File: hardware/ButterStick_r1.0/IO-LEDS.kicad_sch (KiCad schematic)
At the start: 20 parts, among them Q1 Q_NMOS_GSD, Q2 Q_NMOS_GSD, Q3 Q_NMOS_GSD

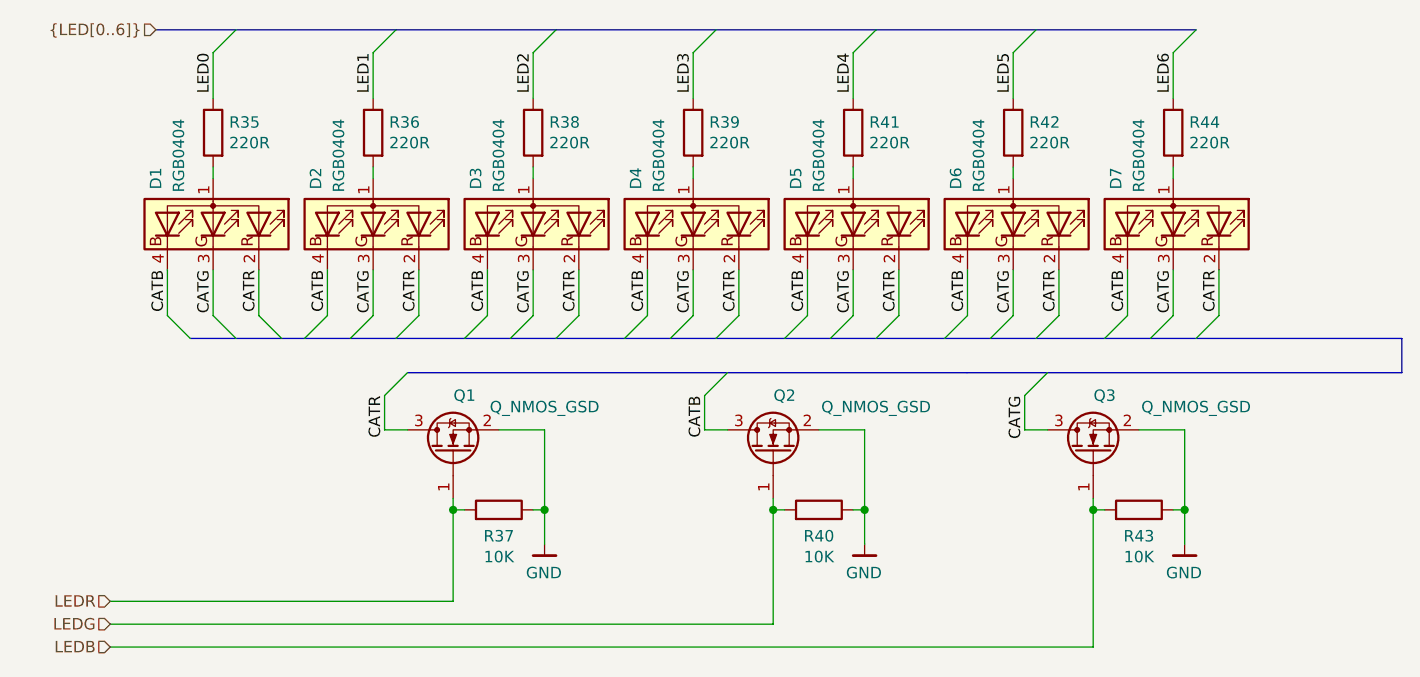
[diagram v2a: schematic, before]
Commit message: hw.r1d0: Fix RGMII straps
This commit correctly sets the stop resistos on the RGMII lines to 1K5
instead of DNP.
Also regenerate and add a schematic in PDF format.

Fixes #6
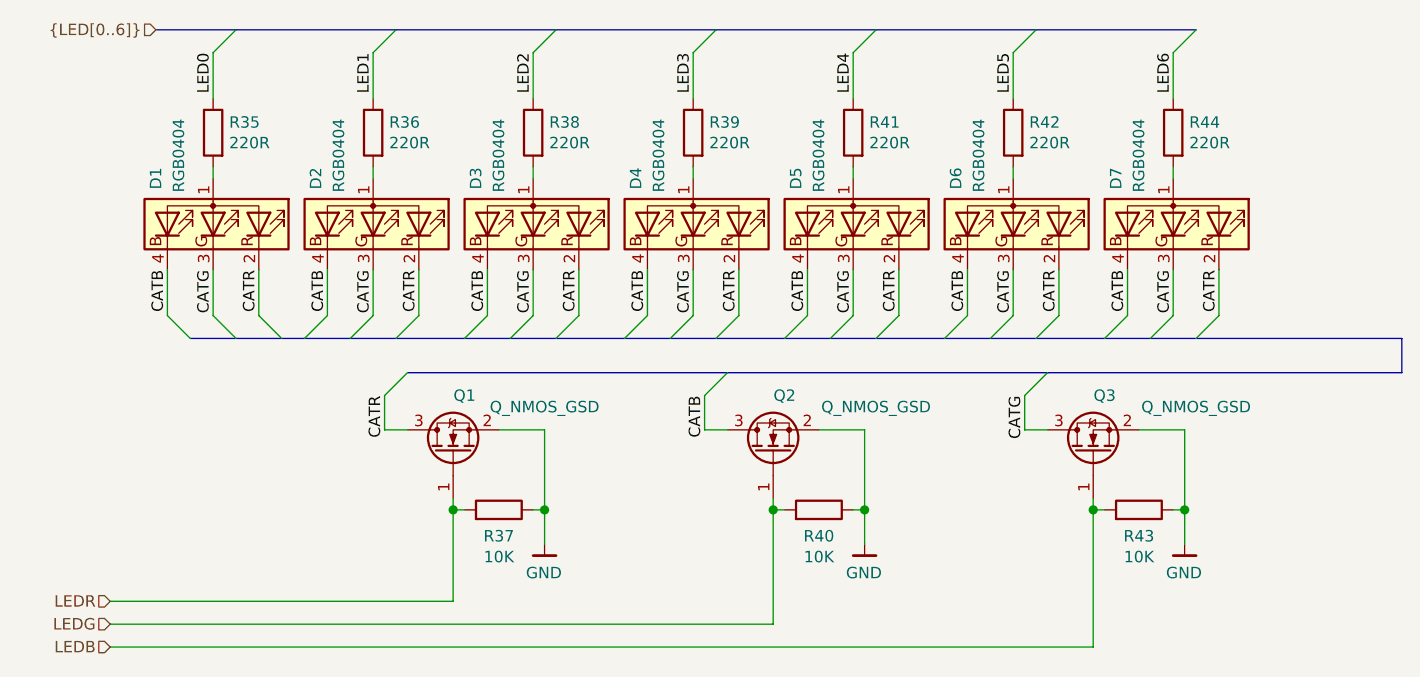
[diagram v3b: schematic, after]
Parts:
- D1, D2, D3, D4, D5, D6, D7: Mfg Foshan NationStar -> MEIHUA; PN FC-B1010RGBT-HG -> MHPA1010RGBDT
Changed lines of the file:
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@@
-(kicad_sch (version 20200618) (host eeschema "5.99.0-unknown-73168a9~101~ubuntu18.04.1")
+(kicad_sch (version 20201015) (generator eeschema)
   (page 1 18)
   (paper "A4")
   (title_block
     (title "ButterStick")
-    (date "2020-07-17")
+    (date "2020-11-01")
     (rev "r1.0")
     (company "GsD")
     (comment 1 "Functional prototyping board for the Lattice ECP5.")
-  )
-  (junction (at 116.84 125.73) (diameter 0) (color 0 0 0 0))
-  (junction (at 127 125.73) (diameter 0) (color 0 0 0 0))
-  (junction (at 152.4 125.73) (diameter 0) (color 0 0 0 0))
-  (junction (at 162.56 125.73) (diameter 0) (color 0 0 0 0))
-  (junction (at 187.96 125.73) (diameter 0) (color 0 0 0 0))
-  (junction (at 198.12 125.73) (diameter 0) (color 0 0 0 0))
+    (comment 2 "SYZYGY compatible")
+  )
+  (junction (at 116.84 125.73) (diameter 1.016) (color 0 0 0 0))
+  (junction (at 127 125.73) (diameter 1.016) (color 0 0 0 0))
+  (junction (at 152.4 125.73) (diameter 1.016) (color 0 0 0 0))
+  (junction (at 162.56 125.73) (diameter 1.016) (color 0 0 0 0))
+  (junction (at 187.96 125.73) (diameter 1.016) (color 0 0 0 0))
+  (junction (at 198.12 125.73) (diameter 1.016) (color 0 0 0 0))
   (bus_entry (at 85.09 104.14) (size 2.54 2.54)
     (stroke (width 0.1524) (type solid) (color 0 0 0 0))
@@
     (stroke (width 0) (type solid) (color 0 0 0 0))
   )
-  (bus (pts (xy 83.82 72.39) (xy 110.49 72.39))
-    (stroke (width 0) (type solid) (color 0 0 0 0))
-  )
-  (bus (pts (xy 87.63 106.68) (xy 97.79 106.68))
+  (bus (pts (xy 83.82 72.39) (xy 92.71 72.39))
+    (stroke (width 0) (type solid) (color 0 0 0 0))
+  )
+  (bus (pts (xy 87.63 106.68) (xy 92.71 106.68))
+    (stroke (width 0) (type solid) (color 0 0 0 0))
+  )
+  (bus (pts (xy 92.71 72.39) (xy 110.49 72.39))
+    (stroke (width 0) (type solid) (color 0 0 0 0))
+  )
+  (bus (pts (xy 92.71 106.68) (xy 97.79 106.68))
     (stroke (width 0) (type solid) (color 0 0 0 0))
   )
@@
     (stroke (width 0) (type solid) (color 0 0 0 0))
   )
-  (bus (pts (xy 100.33 106.68) (xy 110.49 106.68))
+  (bus (pts (xy 100.33 106.68) (xy 105.41 106.68))
+    (stroke (width 0) (type solid) (color 0 0 0 0))
+  )
+  (bus (pts (xy 105.41 106.68) (xy 110.49 106.68))
     (stroke (width 0) (type solid) (color 0 0 0 0))
   )
@@
     (stroke (width 0) (type solid) (color 0 0 0 0))
   )
-  (bus (pts (xy 111.76 110.49) (xy 173.99 110.49))
-    (stroke (width 0) (type solid) (color 0 0 0 0))
-  )
-  (bus (pts (xy 118.11 106.68) (xy 128.27 106.68))
-    (stroke (width 0) (type solid) (color 0 0 0 0))
-  )
-  (bus (pts (xy 128.27 72.39) (xy 163.83 72.39))
+  (bus (pts (xy 111.76 110.49) (xy 147.32 110.49))
+    (stroke (width 0) (type solid) (color 0 0 0 0))
+  )
+  (bus (pts (xy 118.11 106.68) (xy 123.19 106.68))
+    (stroke (width 0) (type solid) (color 0 0 0 0))
+  )
+  (bus (pts (xy 123.19 106.68) (xy 128.27 106.68))
+    (stroke (width 0) (type solid) (color 0 0 0 0))
+  )
+  (bus (pts (xy 128.27 72.39) (xy 146.05 72.39))
     (stroke (width 0) (type solid) (color 0 0 0 0))
   )
@@
     (stroke (width 0) (type solid) (color 0 0 0 0))
   )
-  (bus (pts (xy 135.89 106.68) (xy 146.05 106.68))
-    (stroke (width 0) (type solid) (color 0 0 0 0))
-  )
-  (bus (pts (xy 146.05 106.68) (xy 158.75 106.68))
-    (stroke (width 0) (type solid) (color 0 0 0 0))
-  )
-  (bus (pts (xy 158.75 106.68) (xy 171.45 106.68))
-    (stroke (width 0) (type solid) (color 0 0 0 0))
-  )
-  (bus (pts (xy 163.83 72.39) (xy 199.39 72.39))
-    (stroke (width 0) (type solid) (color 0 0 0 0))
-  )
-  (bus (pts (xy 171.45 106.68) (xy 181.61 106.68))
-    (stroke (width 0) (type solid) (color 0 0 0 0))
-  )
-  (bus (pts (xy 173.99 110.49) (xy 222.25 110.49))
-    (stroke (width 0) (type solid) (color 0 0 0 0))
-  )
-  (bus (pts (xy 181.61 106.68) (xy 194.31 106.68))
-    (stroke (width 0) (type solid) (color 0 0 0 0))
-  )
-  (bus (pts (xy 194.31 106.68) (xy 222.25 106.68))
+  (bus (pts (xy 135.89 106.68) (xy 140.97 106.68))
+    (stroke (width 0) (type solid) (color 0 0 0 0))
+  )
+  (bus (pts (xy 140.97 106.68) (xy 146.05 106.68))
+    (stroke (width 0) (type solid) (color 0 0 0 0))
+  )
+  (bus (pts (xy 146.05 72.39) (xy 163.83 72.39))
+    (stroke (width 0) (type solid) (color 0 0 0 0))
+  )
+  (bus (pts (xy 146.05 106.68) (xy 153.67 106.68))
+    (stroke (width 0) (type solid) (color 0 0 0 0))
+  )
+  (bus (pts (xy 147.32 110.49) (xy 182.88 110.49))
+    (stroke (width 0) (type solid) (color 0 0 0 0))
+  )
+  (bus (pts (xy 153.67 106.68) (xy 158.75 106.68))
+    (stroke (width 0) (type solid) (color 0 0 0 0))
+  )
+  (bus (pts (xy 158.75 106.68) (xy 163.83 106.68))
+    (stroke (width 0) (type solid) (color 0 0 0 0))
+  )
+  (bus (pts (xy 163.83 72.39) (xy 181.61 72.39))
+    (stroke (width 0) (type solid) (color 0 0 0 0))
+  )
+  (bus (pts (xy 163.83 106.68) (xy 171.45 106.68))
+    (stroke (width 0) (type solid) (color 0 0 0 0))
+  )
+  (bus (pts (xy 171.45 106.68) (xy 176.53 106.68))
+    (stroke (width 0) (type solid) (color 0 0 0 0))
+  )
+  (bus (pts (xy 176.53 106.68) (xy 181.61 106.68))
+    (stroke (width 0) (type solid) (color 0 0 0 0))
+  )
+  (bus (pts (xy 181.61 72.39) (xy 199.39 72.39))
+    (stroke (width 0) (type solid) (color 0 0 0 0))
+  )
+  (bus (pts (xy 181.61 106.68) (xy 189.23 106.68))
+    (stroke (width 0) (type solid) (color 0 0 0 0))
+  )
+  (bus (pts (xy 182.88 110.49) (xy 222.25 110.49))
+    (stroke (width 0) (type solid) (color 0 0 0 0))
+  )
+  (bus (pts (xy 189.23 106.68) (xy 194.31 106.68))
+    (stroke (width 0) (type solid) (color 0 0 0 0))
+  )
+  (bus (pts (xy 194.31 106.68) (xy 199.39 106.68))
+    (stroke (width 0) (type solid) (color 0 0 0 0))
+  )
+  (bus (pts (xy 199.39 106.68) (xy 222.25 106.68))
     (stroke (width 0) (type solid) (color 0 0 0 0))
   )
@@
       (effects (font (size 1.27 1.27)) hide)
     )
-    (property "PN" "FC-B1010RGBT-HG" (id 5) (at 90.17 93.98 0)
-      (effects (font (size 1.27 1.27)) hide)
-    )
-    (property "Mfg" "Foshan NationStar" (id 4) (at 90.17 93.98 0)
+    (property "PN" "MHPA1010RGBDT" (id 5) (at 90.17 93.98 0)
+      (effects (font (size 1.27 1.27)) hide)
+    )
+    (property "Mfg" "MEIHUA" (id 4) (at 90.17 93.98 0)
       (effects (font (size 1.27 1.27)) hide)
     )
@@
       (effects (font (size 1.27 1.27)) hide)
     )
-    (property "PN" "FC-B1010RGBT-HG" (id 5) (at 107.95 93.98 0)
-      (effects (font (size 1.27 1.27)) hide)
-    )
-    (property "Mfg" "Foshan NationStar" (id 4) (at 107.95 93.98 0)
+    (property "PN" "MHPA1010RGBDT" (id 5) (at 107.95 93.98 0)
+      (effects (font (size 1.27 1.27)) hide)
+    )
+    (property "Mfg" "MEIHUA" (id 4) (at 107.95 93.98 0)
       (effects (font (size 1.27 1.27)) hide)
     )
@@
       (effects (font (size 1.27 1.27)) hide)
     )
-    (property "PN" "FC-B1010RGBT-HG" (id 5) (at 125.73 93.98 0)
-      (effects (font (size 1.27 1.27)) hide)
-    )
-    (property "Mfg" "Foshan NationStar" (id 4) (at 125.73 93.98 0)
+    (property "PN" "MHPA1010RGBDT" (id 5) (at 125.73 93.98 0)
+      (effects (font (size 1.27 1.27)) hide)
+    )
+    (property "Mfg" "MEIHUA" (id 4) (at 125.73 93.98 0)
       (effects (font (size 1.27 1.27)) hide)
     )
@@
       (effects (font (size 1.27 1.27)) hide)
     )
-    (property "PN" "FC-B1010RGBT-HG" (id 5) (at 143.51 93.98 0)
-      (effects (font (size 1.27 1.27)) hide)
-    )
-    (property "Mfg" "Foshan NationStar" (id 4) (at 143.51 93.98 0)
+    (property "PN" "MHPA1010RGBDT" (id 5) (at 143.51 93.98 0)
+      (effects (font (size 1.27 1.27)) hide)
+    )
+    (property "Mfg" "MEIHUA" (id 4) (at 143.51 93.98 0)
       (effects (font (size 1.27 1.27)) hide)
     )
@@
       (effects (font (size 1.27 1.27)) hide)
     )
-    (property "PN" "FC-B1010RGBT-HG" (id 5) (at 161.29 93.98 0)
-      (effects (font (size 1.27 1.27)) hide)
-    )
-    (property "Mfg" "Foshan NationStar" (id 4) (at 161.29 93.98 0)
+    (property "PN" "MHPA1010RGBDT" (id 5) (at 161.29 93.98 0)
+      (effects (font (size 1.27 1.27)) hide)
+    )
+    (property "Mfg" "MEIHUA" (id 4) (at 161.29 93.98 0)
       (effects (font (size 1.27 1.27)) hide)
     )
@@
       (effects (font (size 1.27 1.27)) hide)
     )
-    (property "PN" "FC-B1010RGBT-HG" (id 5) (at 179.07 93.98 0)
-      (effects (font (size 1.27 1.27)) hide)
-    )
-    (property "Mfg" "Foshan NationStar" (id 4) (at 179.07 93.98 0)
+    (property "PN" "MHPA1010RGBDT" (id 5) (at 179.07 93.98 0)
+      (effects (font (size 1.27 1.27)) hide)
+    )
+    (property "Mfg" "MEIHUA" (id 4) (at 179.07 93.98 0)
       (effects (font (size 1.27 1.27)) hide)
     )
@@
       (effects (font (size 1.27 1.27)) hide)
     )
-    (property "PN" "FC-B1010RGBT-HG" (id 5) (at 196.85 93.98 0)
-      (effects (font (size 1.27 1.27)) hide)
-    )
-    (property "Mfg" "Foshan NationStar" (id 4) (at 196.85 93.98 0)
-      (effects (font (size 1.27 1.27)) hide)
-    )
+    (property "PN" "MHPA1010RGBDT" (id 5) (at 196.85 93.98 0)
+      (effects (font (size 1.27 1.27)) hide)
+    )
+    (property "Mfg" "MEIHUA" (id 4) (at 196.85 93.98 0)
+      (effects (font (size 1.27 1.27)) hide)
+    )

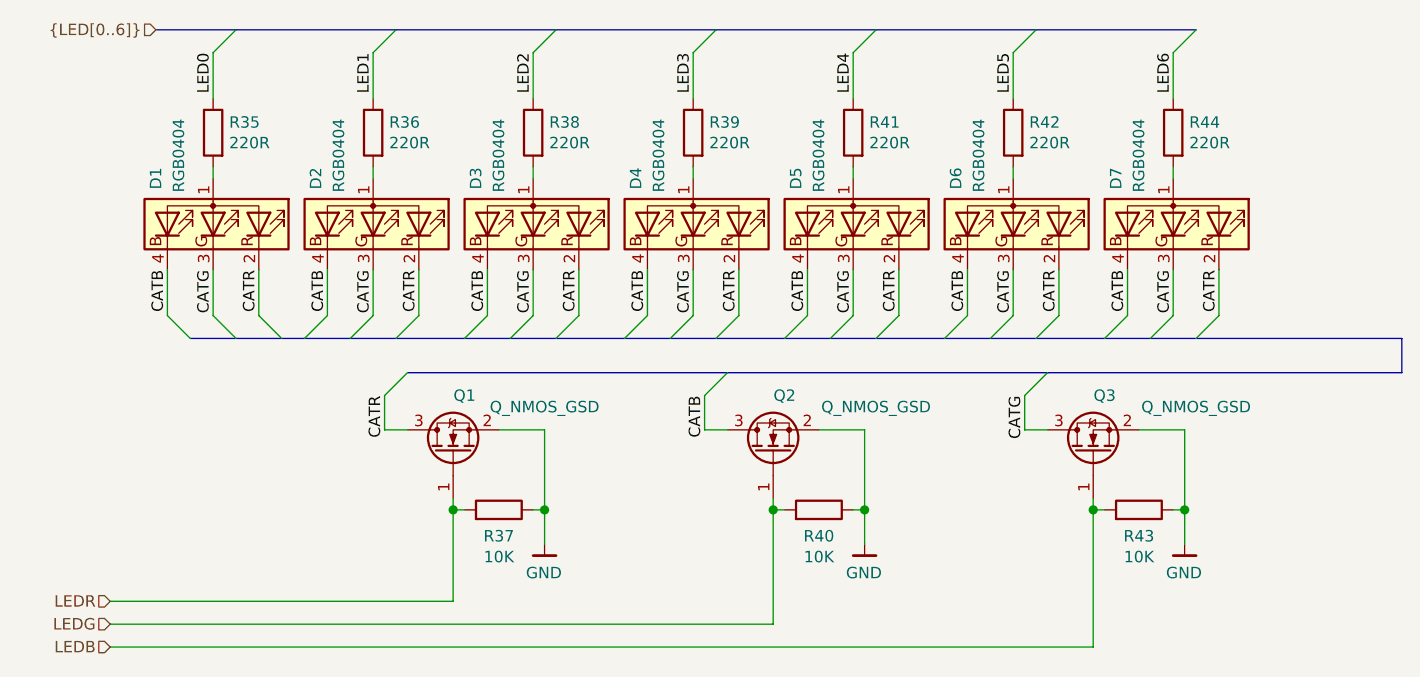
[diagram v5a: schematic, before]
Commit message: Fix RGB G/B signals
- Corrects a mistake where blue and green signals were swapped
- Regenerate schematic

Closes #12
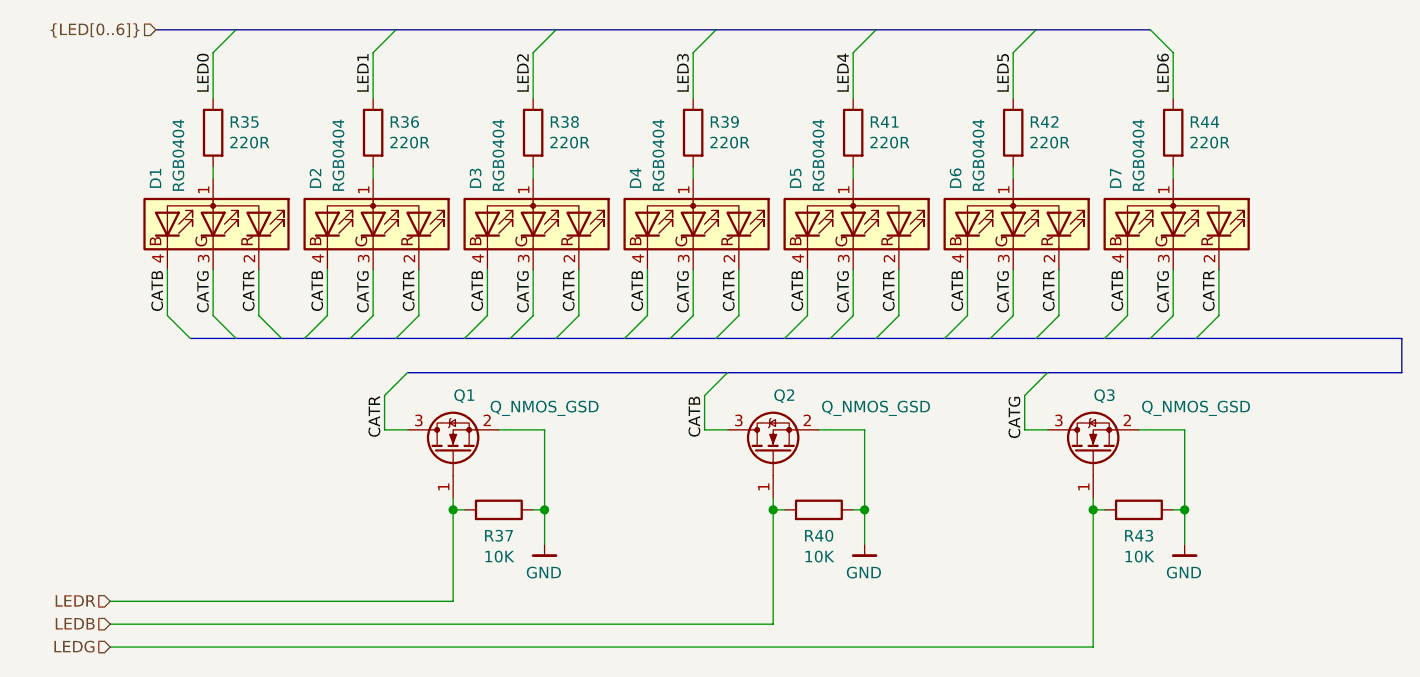
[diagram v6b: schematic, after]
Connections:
- net LEDB: now also Q2.1 (G), R40.2; no longer Q3.1 (G), R43.2
- net LEDG: now also Q3.1 (G), R43.2; no longer Q2.1 (G), R40.2
